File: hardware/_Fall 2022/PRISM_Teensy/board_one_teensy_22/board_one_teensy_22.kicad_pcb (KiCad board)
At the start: 2 copper layers, 61 x 88.9 mm, 21 parts, among them J1 EAST, J2 CORE_IO, J3 USB_micro, U1 Teensy4.1, U2 BNO055_Breakout, U3 3966

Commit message: PRISM_FC jlc files
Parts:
- moved ? 0.16 mm to (138.1, 134.5)
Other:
- board text added: "Ari Bobesh Charlie Babe Jiayuan Liu Lili Baker Rowan Jansens"
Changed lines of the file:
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@@
       (outputformat 1)
       (mirror false)
-      (drillshape 1)
+      (drillshape 0)
       (scaleselection 1)
-      (outputdirectory "")
+      (outputdirectory "JLC/")
     )
   )
@@
       (effects (font (size 1 1) (thickness 0.15)))
     )
-    (fp_text value "CORE_IO" (at 6 7.838 90) (layer "F.SilkS")
+    (fp_text value "CORE_IO" (at 6 7.838 90) (layer "F.SilkS") hide
       (effects (font (size 1 1) (thickness 0.15)))
     )
@@
     (fp_line (start -1.25 -1.35) (end -1.95 -1.35) (layer "F.Fab") (width 0.1))
     (fp_line (start 13.25 0.25) (end -1.25 0.25) (layer "F.Fab") (width 0.1))
-    (pad "1" thru_hole roundrect (at 0 0 270) (size 1.2 1.75) (drill 0.75) (layers *.Cu *.Mask) (roundrect_rratio 0.208333)
+    (pad "1" thru_hole roundrect (at 0 0 270) (size 1.2 1.75) (drill 0.75) (layers *.Cu *.Mask) (roundrect_rratio 0.2083333333)
       (net 2 "GND") (pinfunction "Pin_1") (pintype "passive"))
     (pad "2" thru_hole oval (at 2 0 270) (size 1.2 1.75) (drill 0.75) (layers *.Cu *.Mask)
@@
     (property "Sheetname" "")
     (attr exclude_from_pos_files)
-    (fp_text reference "H3" (at 0 -3.8) (layer "F.SilkS")
+    (fp_text reference "H3" (at 0 -3.8) (layer "F.SilkS") hide
       (effects (font (size 1 1) (thickness 0.15)))
     )
@@
     (property "Sheetname" "")
     (attr through_hole)
-    (fp_text reference "U2" (at 0 -0.386 90) (layer "F.SilkS")
+    (fp_text reference "U2" (at -0.25 -0.3352 90) (layer "F.SilkS")
       (effects (font (size 1 1) (thickness 0.15)))
     )
@@
   )
   (footprint "LOGO" (layer "F.Cu")
-    (at 138.176 134.62)
+    (at 138.1252 134.4676)
     (attr board_only exclude_from_pos_files exclude_from_bom)
     (fp_text reference "" (at 0 0) (layer "F.SilkS")
@@
       (effects (font (size 1 1) (thickness 0.15)))
     )
-    (fp_text value "EAST" (at 3 8.122) (layer "F.SilkS")
+    (fp_text value "EAST" (at 3 8.122) (layer "F.SilkS") hide
       (effects (font (size 1 1) (thickness 0.15)))
     )
@@
     (fp_line (start 0 0.875) (end -0.5 1.375) (layer "F.Fab") (width 0.1))
     (fp_line (start -1.25 -1.35) (end -1.95 -1.35) (layer "F.Fab") (width 0.1))
-    (pad "1" thru_hole roundrect (at 0 0 180) (size 1.2 1.75) (drill 0.75) (layers *.Cu *.Mask) (roundrect_rratio 0.208333)
+    (pad "1" thru_hole roundrect (at 0 0 180) (size 1.2 1.75) (drill 0.75) (layers *.Cu *.Mask) (roundrect_rratio 0.2083333333)
       (net 2 "GND") (pinfunction "Pin_1") (pintype "passive"))
     (pad "2" thru_hole oval (at 2 0 180) (size 1.2 1.75) (drill 0.75) (layers *.Cu *.Mask)
@@
   (gr_arc (start 127.11 120.23) (mid 129.23132 121.10868) (end 130.11 123.23) (layer "Edge.Cuts") (width 0.2))
   (gr_line (start 138.11 130.484) (end 139.61 130.484) (layer "Edge.Cuts") (width 0.2))
+  (gr_text "Ari Bobesh\nCharlie Babe\nJiayuan Liu\nLili Baker\nRowan Jansens" (at 155.702 85.0392) (layer "B.SilkS")
+    (effects (font (size 1.2 1.2) (thickness 0.15)) (justify mirror))
+  )
   (segment (start 143.764 59.182) (end 143.502 58.92) (width 0.508) (layer "F.Cu") (net 1))
   (segment (start 143.502 58.92) (end 121.71 58.92) (width 0.508) (layer "F.Cu") (net 1))

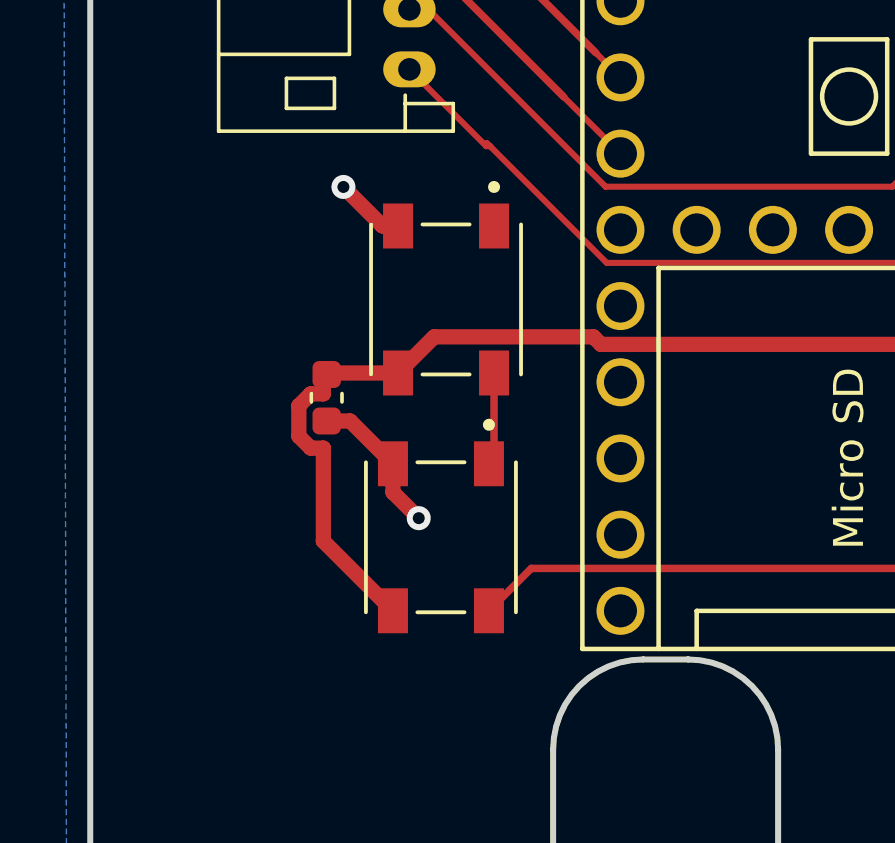
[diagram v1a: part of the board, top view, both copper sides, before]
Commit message: Changed neopixel footprint
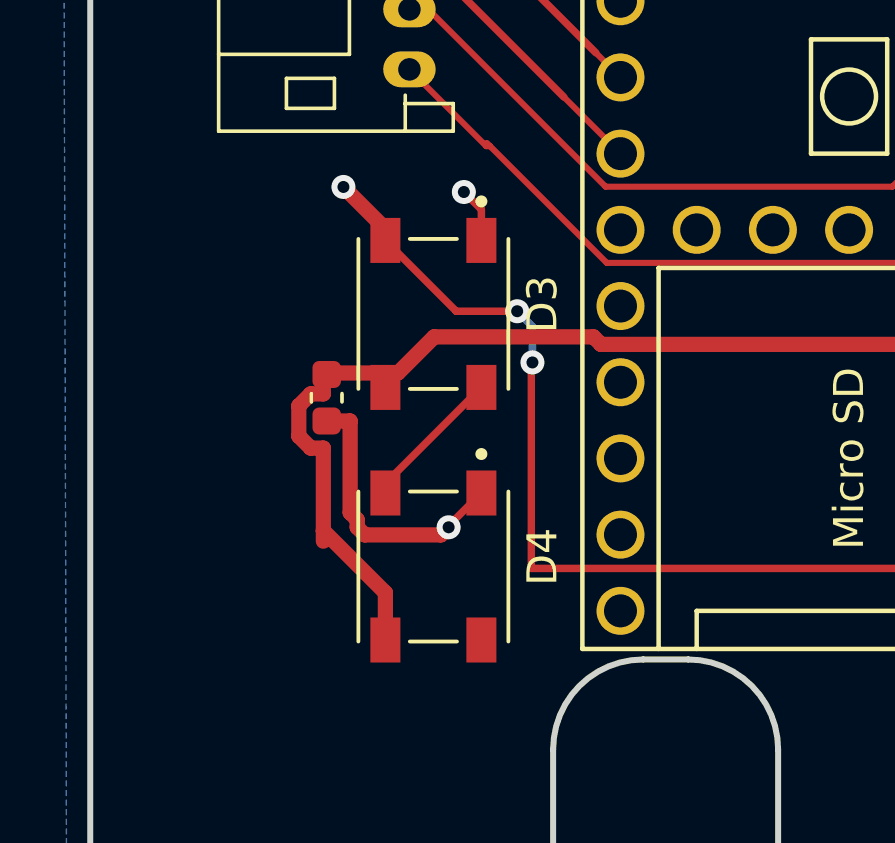
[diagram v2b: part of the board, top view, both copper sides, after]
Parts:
- removed D5: Neopixel2, neopixel:LED_1655
- added D3: 1655, neopixel:LED_1655, F.Cu at (118.6, 108.7)
- D4: value Neopixel1 -> 1655
- moved D4 1.01 mm to (118.6, 117.1)
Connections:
- D4 pad 1: Net-(D4-Pad1) -> GND
- D4 pad 2: GND -> Net-(D3-Pad4)
- D4 pad 4: /NEOPIXEL -> unconnected-(D4-Pad4)
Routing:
- net /NEOPIXEL: track 20.7 -> 34.9 mm, vias 0 -> 3
- net Net-(D3-Pad4): track 0.00 -> 4.85 mm
- net GND: track 31.2 -> 35.0 mm
- net Net-(D4-Pad1): track 3.10 -> 0.00 mm
- net /3.3V: track 118.4 -> 119.6 mm
